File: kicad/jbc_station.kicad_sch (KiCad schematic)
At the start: 73 parts, among them J19 Conn_01x05, U1 STM32F401CCUx, U10 HT7463, U11 L78L05_SOT89, U12 LP2985-3.3, U13 ICL7660, U14 M24C64, U8 INA3221, U9 HT7463, Y1 Crystal

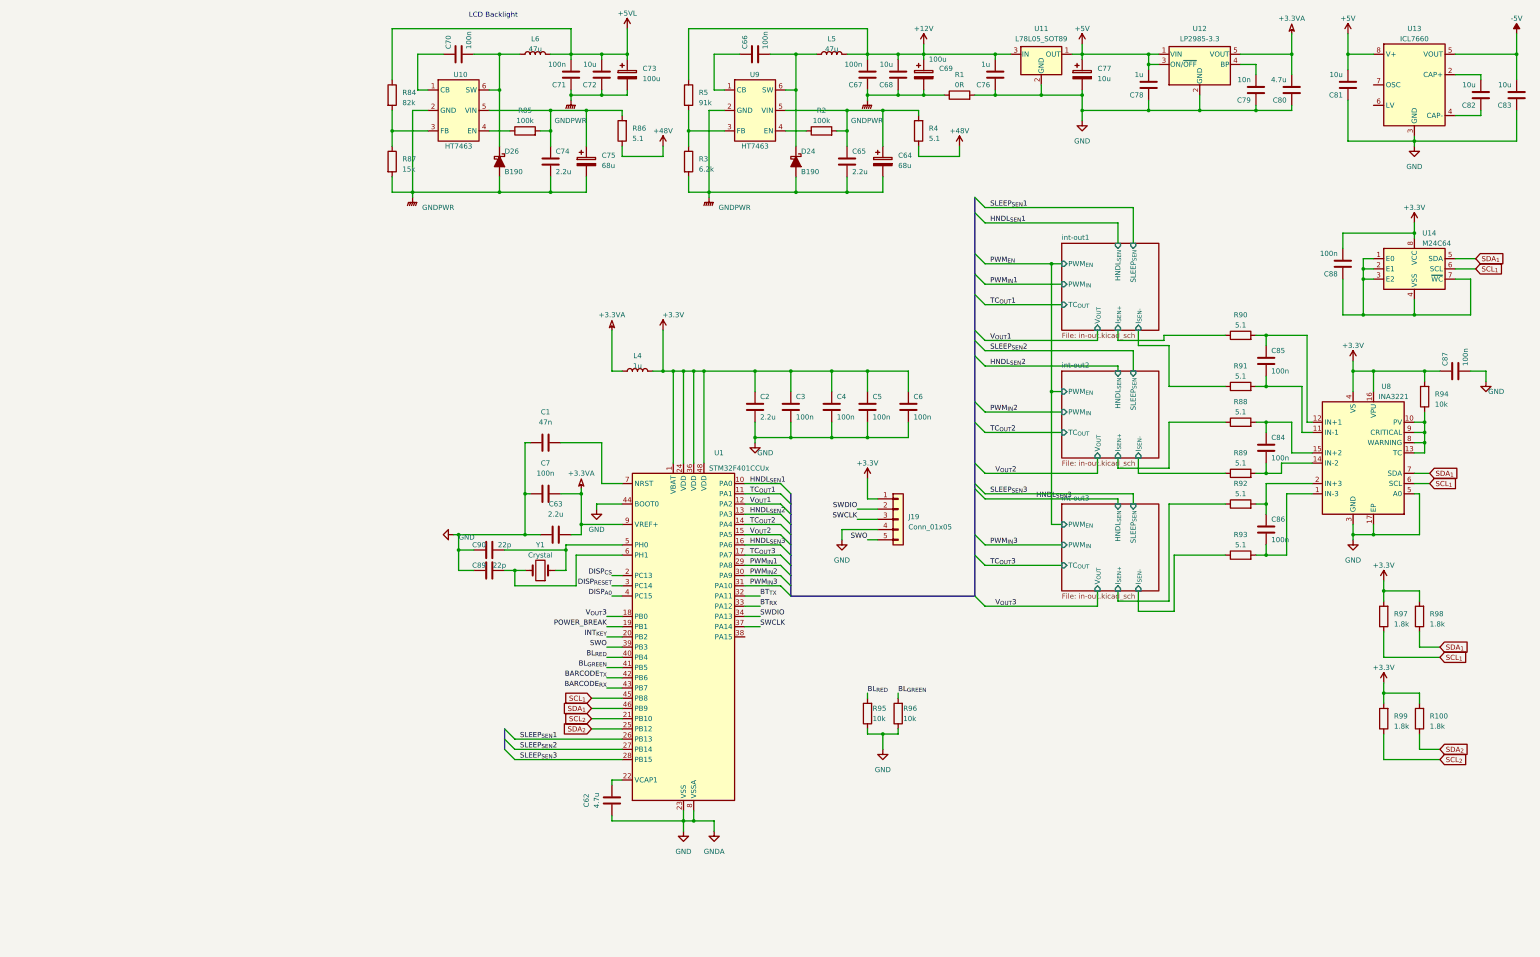
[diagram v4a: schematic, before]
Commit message: Main board: add BT
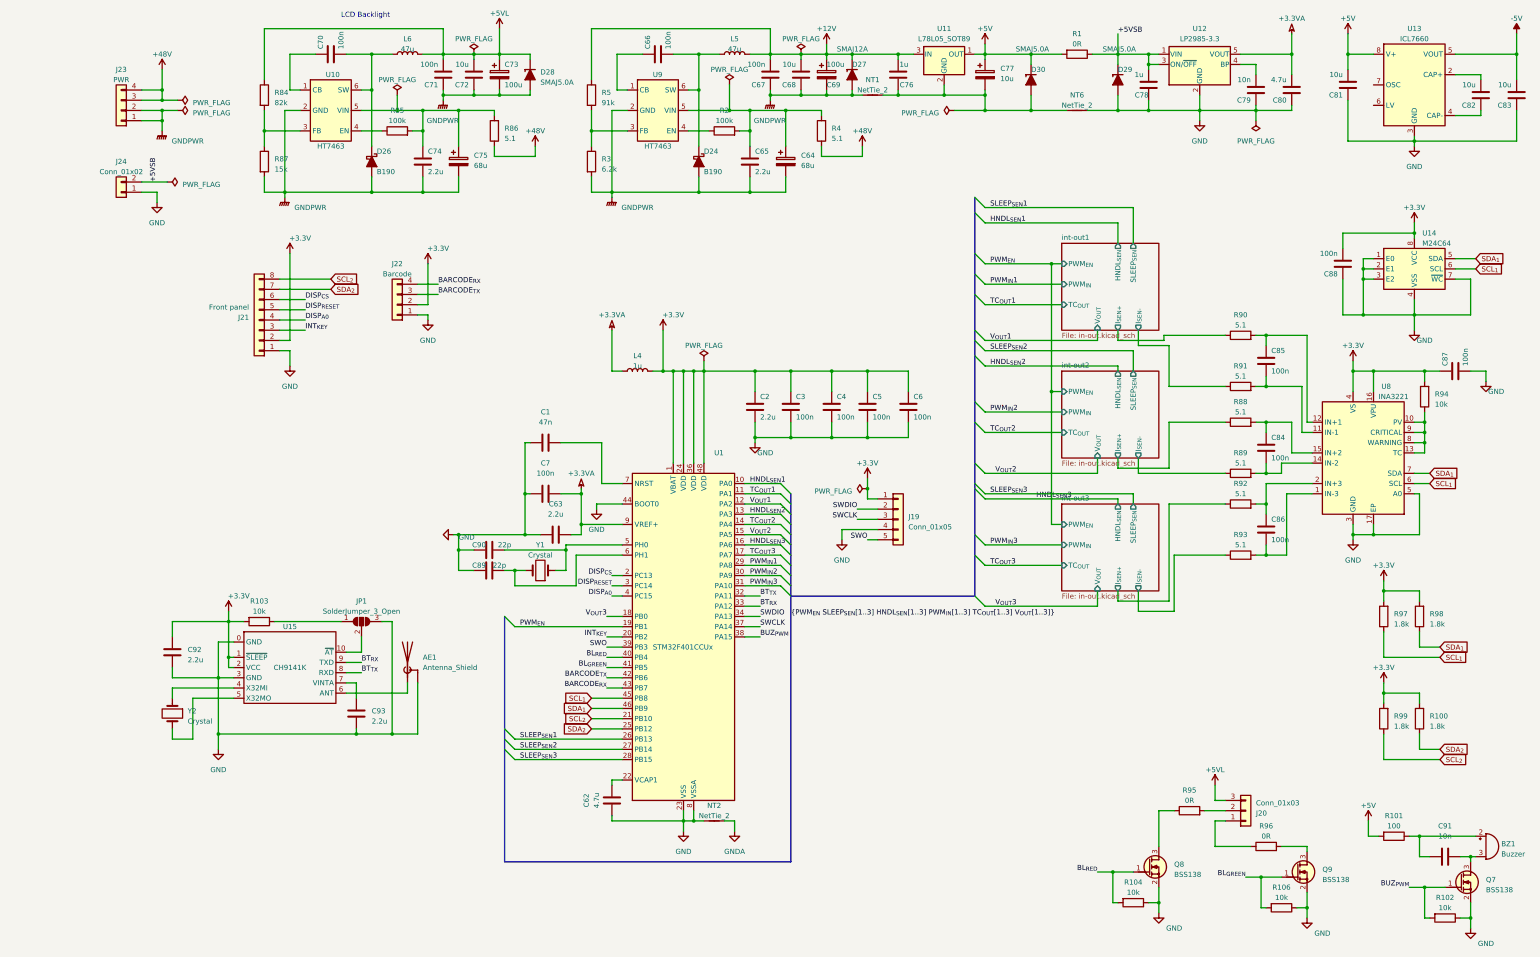
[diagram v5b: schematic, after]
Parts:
- removed R1: 0R_0603, 4ms_Resistor:R_0603, symbol PCM_4ms_Resistor:0R_0603
- added AE1: Antenna_Shield, RF_Antenna:Texas_SWRA117D_2.4GHz_Left, symbol Device:Antenna_Shield
- added BZ1: Buzzer, Footprints:BUZ_5020, symbol Device:Buzzer
- added C91: 10n, Capacitor_SMD:C_0805_2012Metric, symbol Device:C
- added C92, C93: 2.2u, Capacitor_SMD:C_1206_3216Metric_Pad1.33x1.80mm_HandSolder, symbol Device:C
- added D27: SMAJ12A, Diode_SMD_AKL:D_SMA, symbol Diode_TVS_AKL:SMAJ12A
- added D28, D29, D30: SMAJ5.0A, Diode_SMD_AKL:D_SMA, symbol Diode_TVS_AKL:SMAJ5.0A
- added J20: Conn_01x03, Connector_JST:JST_EH_B3B-EH-A_1x03_P2.50mm_Vertical, symbol Connector_Generic:Conn_01x03
- added J21: Front panel, Connector_JST:JST_EH_B8B-EH-A_1x08_P2.50mm_Vertical, symbol Connector_Generic:Conn_01x08
- added J22: Barcode, Connector_JST:JST_EH_B4B-EH-A_1x04_P2.50mm_Vertical, symbol Connector_Generic:Conn_01x04
- added J23: PWR, Connector_Molex:Molex_KK-254_AE-6410-04A_1x04_P2.54mm_Vertical, symbol Connector_Generic:Conn_01x04
- added J24: Conn_01x02, Connector_JST:JST_EH_B2B-EH-A_1x02_P2.50mm_Vertical, symbol Connector_Generic:Conn_01x02
- added JP1: SolderJumper_3_Open, Jumper:SolderJumper-3_P2.0mm_Open_TrianglePad1.0x1.5mm_NumberLabels, symbol Jumper:SolderJumper_3_Open
- added NT1, NT2, NT6: NetTie_2, NetTie:NetTie-2_SMD_Pad2.0mm, symbol Device:NetTie_2
- added Q7, Q8, Q9: BSS138, Package_TO_SOT_SMD_AKL:SOT-23, symbol Transistor_MOSFET_AKL:BSS138
- added R1: 0R, Jumper:SolderJumper-2_P1.3mm_Open_TrianglePad1.0x1.5mm, symbol Device:R
- added R101: 100, Resistor_SMD:R_0805_2012Metric_Pad1.20x1.40mm_HandSolder, symbol Device:R
- added R102, R103, R104, R106: 10k, Resistor_SMD:R_0805_2012Metric_Pad1.20x1.40mm_HandSolder, symbol Device:R
- added U15: CH9141K, Footprints:ESSOP-10_3.9x4.9mm_P1.00mm, symbol custom_symbols:CH9141K
- added Y2: Crystal, Crystal:Crystal_SMD_3225-4Pin_3.2x2.5mm_HandSoldering, symbol Device:Crystal
- C3, C4, C5, C6, C7: footprint Capacitor_SMD:C_0805_2012Metric -> Capacitor_SMD:C_0603_1608Metric_Pad1.08x0.95mm_HandSolder
- C64, C69, C73, C75: footprint (none) -> Capacitor_THT:C_Radial_D8.0mm_H11.5mm_P3.50mm
- C77: footprint (none) -> Capacitor_SMD:C_1812_4532Metric
- D24, D26: symbol PCM_Diode_Schottky_AKL:B190 -> Diode_Schottky_AKL:B190
- J19: footprint (none) -> Connector_PinHeader_2.54mm:PinHeader_1x05_P2.54mm_Vertical
- L4: footprint (none) -> Inductor_SMD:L_1206_3216Metric_Pad1.22x1.90mm_HandSolder
- L5, L6: footprint (none) -> Inductor_SMD:L_7.3x7.3_H3.5
- R100, R2, R3, R5, R84, R85, R87, R94, R97, R98, R99: footprint (none) -> Resistor_SMD:R_0603_1608Metric_Pad0.98x0.95mm_HandSolder
- R4, R86: footprint (none) -> Resistor_SMD:R_1206_3216Metric_Pad1.30x1.75mm_HandSolder
- R88, R89, R90, R91, R92, R93: footprint (none) -> Resistor_SMD:R_0805_2012Metric_Pad1.20x1.40mm_HandSolder
- R95, R96: value 10k -> 0R; footprint (none) -> Resistor_SMD:R_1206_3216Metric_Pad1.30x1.75mm_HandSolder
- U13: footprint (none) -> Package_SO:SOIC-8_3.9x4.9mm_P1.27mm
- Y1: footprint PCM_Crystal_AKL:Crystal_SMD_MicroCrystal_MS1V-T1K -> Crystal_AKL:Crystal_SMD_MicroCrystal_MS1V-T1K
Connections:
- net POWER_BREAK is gone; now on net PWM_{EN}: U1.19 (PB1)
- net +12V: now also D27.1 (K)
- net +3.3V: now also C92.2, J21.2 (Pin_2), J22.2 (Pin_2), R103.2, U15.1 (~{SLEEP}), U15.2 (VCC)
- net +48V: now also J23.3 (Pin_3), J23.4 (Pin_4)
- net +5V: now also D30.1 (K), R1.2, R101.2; no longer C78.2, U12.1 (VIN), U12.3 (ON/~{OFF})
- net +5VL: now also D28.1 (K), J20.3 (Pin_3)
- net BARCODE_{RX}: now also J22.4 (Pin_4)
- net BARCODE_{TX}: now also J22.3 (Pin_3)
- net BL_{GREEN}: now also Q9.1 (G), R106.2; no longer R96.2
- net BL_{RED}: now also Q8.1 (G), R104.2; no longer R95.2
- net BT_{RX}: now also U15.9 (TXD)
- net BT_{TX}: now also U15.8 (RXD)
- net DISP_{A0}: now also J21.4 (Pin_4)
- net DISP_{CS}: now also J21.6 (Pin_6)
- net DISP_{RESET}: now also J21.5 (Pin_5)
- net GND: now also C88.1, U14.1 (E0), U14.2 (E1), U14.3 (E2), U14.4 (VSS), U14.7 (~{WC}), AE1.2 (Shield), C92.1, C93.1, D29.2 (A), J21.1 (Pin_1), J22.1 (Pin_1), J24.1 (Pin_1), JP1.3 (B), NT2.1, NT6.2, Q7.2 (S), Q8.2 (S), Q9.2 (S), R102.1, R104.1, R106.1, U15.0 (GND), U15.3 (GND); no longer C76.1, C77.2, R95.1, R96.1, U11.2 (GND)
- net GNDPWR: now also D27.2 (A), D28.2 (A), J23.1 (Pin_1), J23.2 (Pin_2), NT1.1
- net INT_{KEY}: now also J21.3 (Pin_3)
- net SCL_{2}: now also J21.8 (Pin_8)
- net SDA_{2}: now also J21.7 (Pin_7)
- net BUZ_{PWM}: now reaches U1.38 (PA15)
- net BUZ_{PWM}: now also Q7.1 (G), R102.2
- new net: J20.1 (Pin_1), R96.1
- new net: Q9.3 (D), R96.2
- new net: BZ1.2 (+), C91.1, R101.1
- new net: Q8.3 (D), R95.1
- new net: J20.2 (Pin_2), R95.2
- new net: C76.1, C77.2, D30.2 (A), NT1.2, NT6.1, U11.2 (GND)
- new net: C93.2, U15.7 (VINTA)
- new net: BZ1.3 (-), C91.2, Q7.3 (D)
- new net: JP1.1 (A), R103.1
- new net: U15.4 (X32MI), Y2.1
- new net: U15.5 (X32MO), Y2.2
- new net: JP1.2 (C), U15.10 (~{AT})
- new net: AE1.1 (A), U15.6 (ANT)
- new net +5VSB: C78.2, D29.1 (K), J24.2 (Pin_2), R1.1, U12.1 (VIN), U12.3 (ON/~{OFF})
- new net GNDA: NT2.2
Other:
- moved on the sheet: C64, C65, C66, C67, C68, C69, C70, C71, C72, C73, C74, C75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

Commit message: PCB routing initial
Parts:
- removed R1: 0R, Jumper:SolderJumper-2_P1.3mm_Open_TrianglePad1.0x1.5mm, symbol Device:R
- added C36: 100n, Capacitor_SMD:C_0603_1608Metric_Pad1.08x0.95mm_HandSolder, symbol Device:C
- added C38, C40: 22p, Capacitor_SMD:C_0805_2012Metric, symbol Device:C
- added F?: Fuse 1A, Fuse:Fuseholder_Littelfuse_Nano2_154x, symbol Device:Fuse
- added H1, H2, H3, H4, H5: MountingHole_Pad, MountingHole:MountingHole_3.2mm_M3_DIN965_Pad_TopBottom, symbol Mechanical:MountingHole_Pad
- added J5: Conn_01x03, Connector_JST:JST_EH_B3B-EH-A_1x03_P2.50mm_Vertical, symbol Connector_Generic:Conn_01x03
- added J7: Conn_01x04, Connector_Molex:Molex_KK-254_AE-6410-04A_1x04_P2.54mm_Vertical, symbol Connector_Generic:Conn_01x04
- added JP1: SolderJumper_2_Bridged, Jumper:SolderJumper-2_P1.3mm_Bridged_RoundedPad1.0x1.5mm, symbol Jumper:SolderJumper_2_Bridged
- added JP2: SolderJumper_2_Open, Jumper:SolderJumper-2_P1.3mm_Open_TrianglePad1.0x1.5mm, symbol Jumper:SolderJumper_2_Open
- added JP3: SolderJumper_3_Bridged12, Jumper:SolderJumper-3_P1.3mm_Bridged12_RoundedPad1.0x1.5mm_NumberLabels, symbol Jumper:SolderJumper_3_Bridged12
- added L3, L5: 1u, Inductor_SMD:L_1206_3216Metric_Pad1.22x1.90mm_HandSolder, symbol Device:L
- added R11, R14, R21: 10k, Resistor_SMD:R_0805_2012Metric_Pad1.20x1.40mm_HandSolder, symbol Device:R
- J1: renamed from J23; footprint Connector_Molex:Molex_KK-254_AE-6410-04A_1x04_P2.54mm_Vertical -> Connector_Phoenix_MC:PhoenixContact_MCV_1,5_4-G-3.5_1x04_P3.50mm_Vertical
- Y1: footprint Crystal_AKL:Crystal_SMD_MicroCrystal_MS1V-T1K -> Crystal_AKL:Crystal_SMD_5032-2Pin_5.0x3.2mm
- renumbered C70 to C1, C77 to C10, C78 to C11, C81 to C12, C79 to C13, C80 to C14, C82 to C15, C83 to C16, C74 to C17, C75 to C18, C65 to C19, C66 to C2, C64 to C20, C88 to C21, C85 to C22, C87 to C23, C2 to C24, C3 to C25, C4 to C26, C5 to C27, C6 to C28, C1 to C29, C71 to C3, C84 to C30, C7 to C31, C86 to C32, C63 to C33, C90 to C34, C89 to C35, C92 to C37, C93 to C39, C72 to C4, C62 to C41, C91 to C42, C73 to C5, C67 to C6, C68 to C7, C69 to C8, C76 to C9, D28 to D1, D27 to D2, D30 to D3, D29 to D4, D26 to D5, D24 to D6, J24 to J2, J22 to J3, J21 to J4, J19 to J6, J20 to J8, JP1 to JP4, L6 to L1, L5 to L2, NT6 to NT2, NT2 to NT3, Q8 to Q1, Q9 to Q2, Q7 to Q3, R84 to R1, R91 to R10, R94 to R12, R88 to R13, R89 to R15, R92 to R16, R93 to R17, R97 to R18, R98 to R19, R5 to R2, R103 to R20, R99 to R22, R100 to R23, R95 to R24, R101 to R25, R96 to R26, R104 to R27, R106 to R28, R102 to R29, R85 to R3, R86 to R4, R2 to R5, R4 to R6, R87 to R7, R3 to R8, R90 to R9, U11 to U1, U12 to U2, U13 to U3, U10 to U4, U9 to U5, U14 to U6, U8 to U7, U1 to U8, U15 to U9
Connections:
- net +3.3V: now also J5.3 (Pin_3), L5.2, R11.1; no longer C37.2, R20.2, U9.1 (~{SLEEP}), U9.2 (VCC)
- net +5V: now also JP1.1 (A)
- net +5VL: now also JP2.2 (B)
- net +5VSB: now also JP1.2 (B), L3.2; no longer J2.2 (Pin_2)
- net BT_{RX}: now also J7.3 (Pin_3)
- net BT_{TX}: now also J7.2 (Pin_2)
- net GND: now also C36.1, C38.2, C40.2, J5.1 (Pin_1), J7.1 (Pin_1), R14.2, R21.2; no longer J2.1 (Pin_1)
- net GNDPWR: now also J2.1 (Pin_1)
- net PWM_{EN}: now also R21.1
- net SWO: now also JP3.2 (C); no longer J6.5 (Pin_5)
- net at U9.4 (X32MI), Y2.1: now also C38.1
- net at U9.5 (X32MO), Y2.2: now also C40.1
- new net: F?.2, JP2.1 (A), L3.1
- new net: C36.2, C37.2, J7.4 (Pin_4), L5.1, R20.2, U9.1 (~{SLEEP}), U9.2 (VCC)
- new net: J6.5 (Pin_5), JP3.3 (B)
- new net: F?.1, J2.2 (Pin_2)
- new net POWER_SW: J5.2 (Pin_2), JP3.1 (A), R11.2, R14.1
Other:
- note added: "Only one of them"
- moved on the sheet: J2

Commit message: Route power stage
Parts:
- removed C28: 100n, Capacitor_SMD:C_0603_1608Metric_Pad1.08x0.95mm_HandSolder, symbol Device:C
- removed D3: SMAJ5.0A, Diode_SMD_AKL:D_SMA, symbol Diode_TVS_AKL:SMAJ5.0A
- removed JP4: SolderJumper_3_Open, Jumper:SolderJumper-3_P2.0mm_Open_TrianglePad1.0x1.5mm_NumberLabels, symbol Jumper:SolderJumper_3_Open
- added C21, C22: 2.2u, Capacitor_SMD:C_0805_2012Metric, symbol Device:C
- added JP3, JP5: SolderJumper_2_Open, Jumper:SolderJumper-2_P1.3mm_Open_TrianglePad1.0x1.5mm, symbol Jumper:SolderJumper_2_Open
- added U6: XC6206PxxxMR, Package_TO_SOT_SMD:SOT-23-3, symbol Regulator_Linear:XC6206PxxxMR
- J7: footprint Connector_Molex:Molex_KK-254_AE-6410-04A_1x04_P2.54mm_Vertical -> Connector_PinHeader_2.54mm:PinHeader_1x04_P2.54mm_Vertical
- renumbered C21 to C23, C22 to C24, C23 to C25, C24 to C26, C25 to C27, C26 to C28, C27 to C29, C29 to C31, C30 to C32, C31 to C33, C32 to C34, C33 to C35, C34 to C36, C35 to C37, C36 to C38, C37 to C39, C38 to C40, C39 to C41, C40 to C42, C41 to C43, C42 to C44, JP3 to JP4, U9 to U10, U6 to U7, U7 to U8, U8 to U9
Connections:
- net +3.3V: now also JP3.2 (B); no longer J3.2 (Pin_2)
- net +5V: now also C22.1, U6.3 (VI)
- net BARCODE_{RX}: now also J3.3 (Pin_3); no longer J3.4 (Pin_4)
- net BARCODE_{TX}: now also J3.2 (Pin_2); no longer J3.3 (Pin_3)
- net GND: now also Y2.2, Y2.4, C21.2, C22.2, JP5.1 (A), U6.1 (GND)
- net at R20.1: now also U10.10 (~{AT}), JP5.2 (B)
- net at C42.1, U10.5 (X32MO): now also Y2.3; no longer Y2.2
- new net: C21.1, J3.4 (Pin_4), JP3.1 (A), U6.2 (VO)
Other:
- moved on the sheet: JP1, NT2

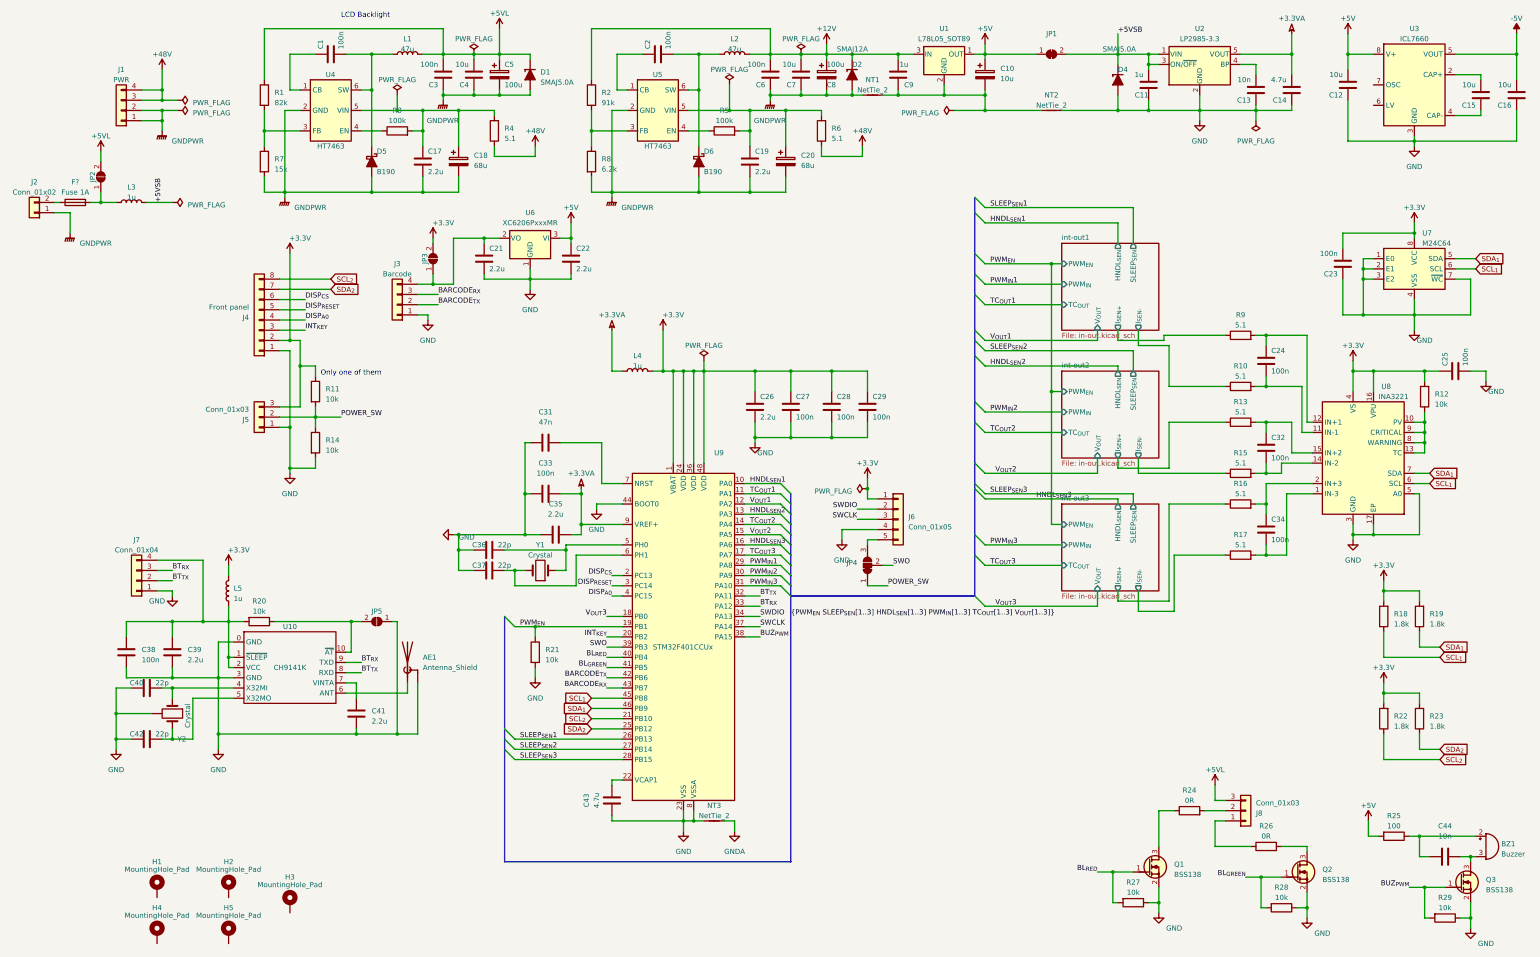
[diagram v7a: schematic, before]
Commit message: Route LDOs
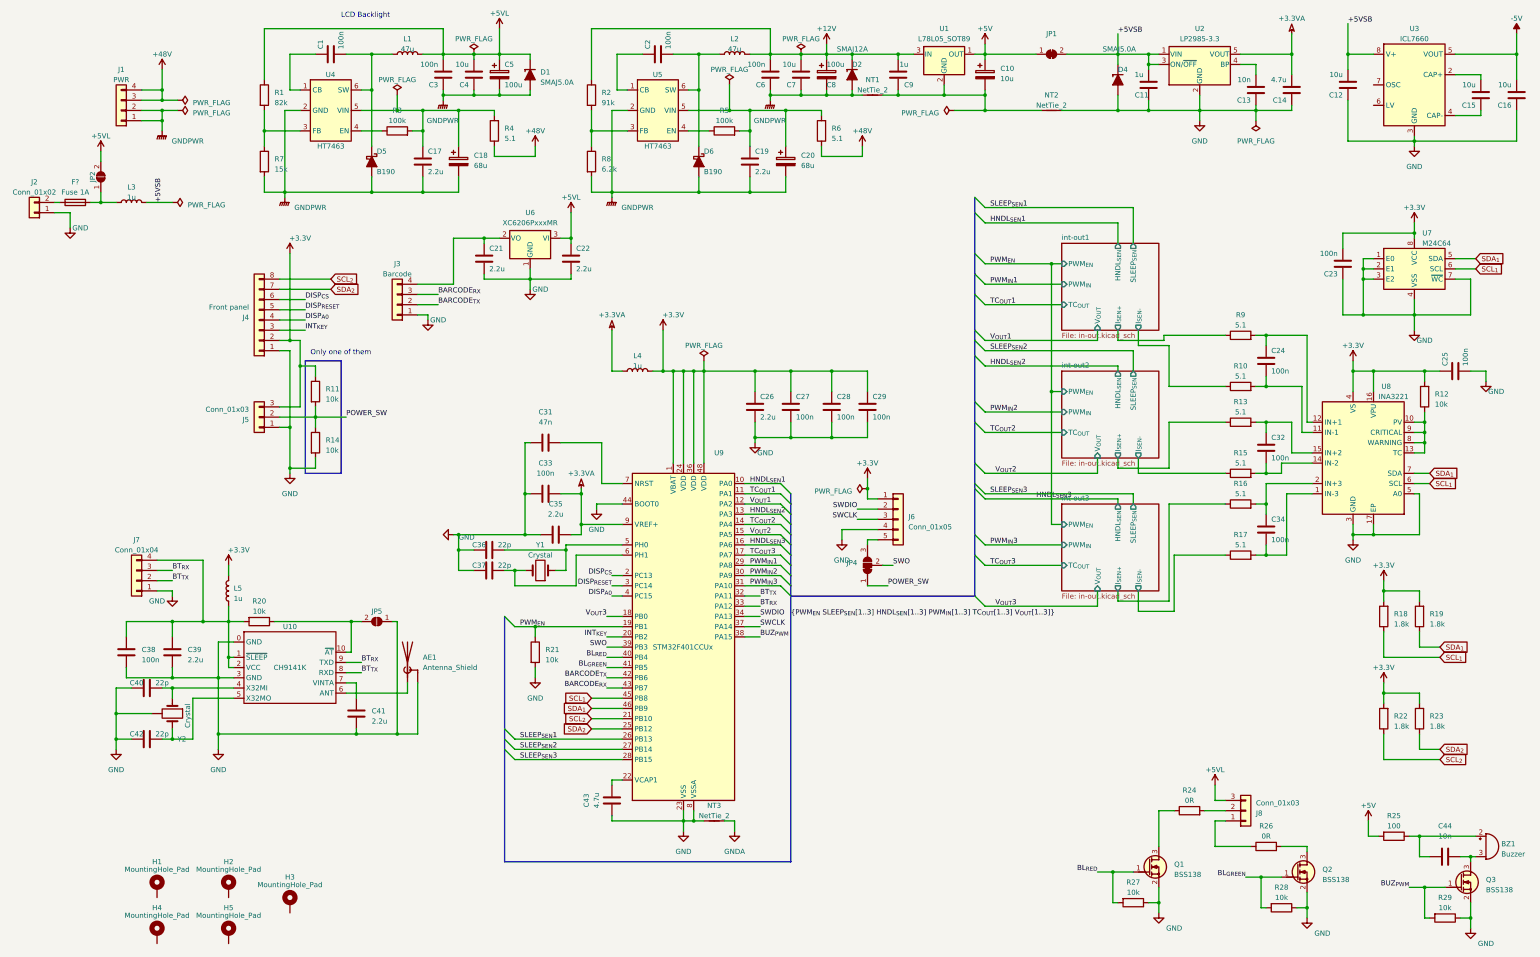
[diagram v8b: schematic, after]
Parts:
- removed JP3: SolderJumper_2_Open, Jumper:SolderJumper-2_P1.3mm_Open_TrianglePad1.0x1.5mm, symbol Jumper:SolderJumper_2_Open
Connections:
- net +5V: no longer C12.2, C22.1, U3.8 (V+), U6.3 (VI)
- net +5VL: now also C22.1, U6.3 (VI)
- net +5VSB: now also C12.2, U3.8 (V+)
- net GND: now also J2.1 (Pin_1)
- net GNDPWR: no longer J2.1 (Pin_1)
